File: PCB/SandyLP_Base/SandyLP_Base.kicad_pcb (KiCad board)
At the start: 2 copper layers, 275.5 x 80.3 mm, 229 parts, among them J1 Conn_01x10_Pin, J7 USB_C_Receptacle_USB2.0, J8 Conn_01x03, Q1 BSS138, SW1 BOOT, SW2 RESET, U1 NCP1117-3.3_SOT223, U2 RP2040, U3 W25Q128JVPIQ, Y1 12MHz

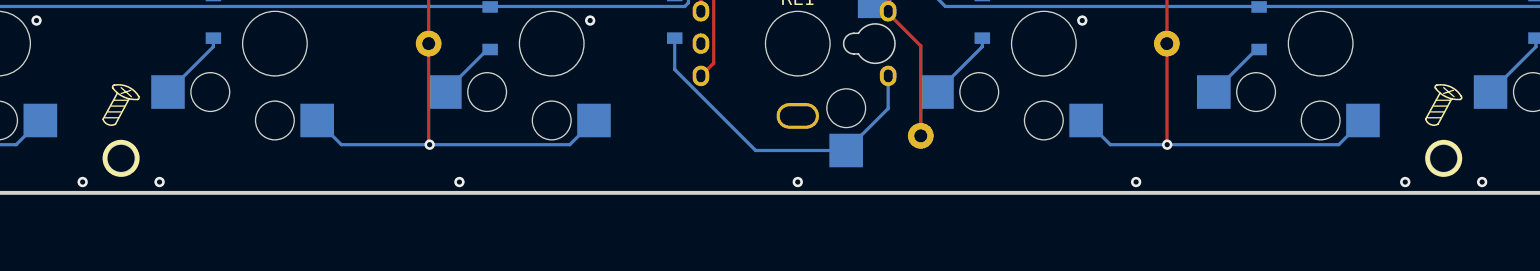
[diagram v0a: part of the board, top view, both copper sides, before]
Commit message: ネジ穴の位置を修正。
ネジ穴の位置が移動したので、シルク位置も調整。
GNDのVIAも位置調整。
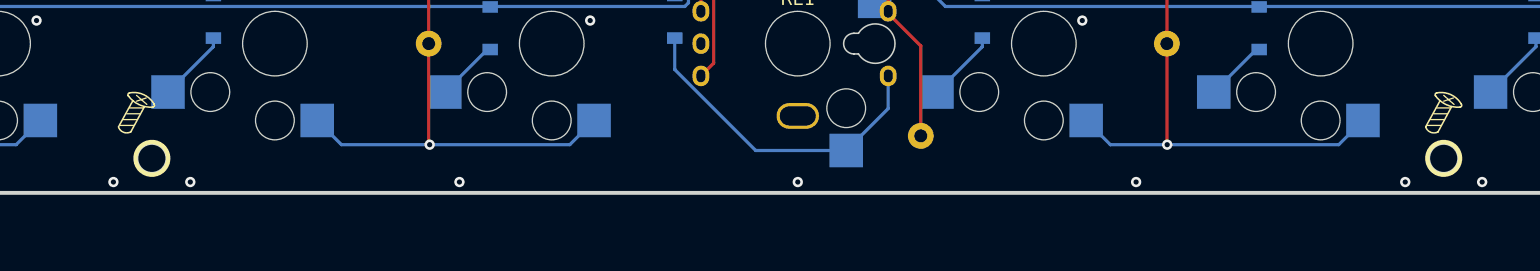
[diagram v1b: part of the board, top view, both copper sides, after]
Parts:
- moved H_btm_9 2.38 mm to (109.2, 112.1)
- moved REF** 1.88 mm to (207.9, 111.3)
- moved REF** 1.33 mm to (107.9, 111.1)
- moved REF** 0.84 mm to (106.7, 111.3)
- moved REF** 0.60 mm to (209.1, 111.1)
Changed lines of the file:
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@@
 		(locked yes)
 		(layer "F.Cu")
-		(at 106.783435 112.08778)
+		(at 109.164685 112.08778)
 		(descr "Mounting Hole 2.2mm, no annular, M2")
 		(tags "mounting hole 2.2mm no annular m2")
@@
 			(polygon
 				(pts
-					(xy 107.783435 109.88778) (xy 108.583435 110.48778) (xy 109.083435 111.28778) (xy 109.183435 112.08778)
-					(xy 109.083435 112.88778) (xy 108.583435 113.68778) (xy 107.783435 114.28778) (xy 106.783435 114.48778)
-					(xy 105.783435 114.28778) (xy 104.983435 113.68778) (xy 104.483435 112.88778) (xy 104.383435 112.08778)
-					(xy 104.483435 111.28778) (xy 104.983435 110.48778) (xy 105.783435 109.88778) (xy 106.783435 109.68778)
+					(xy 110.164685 109.88778) (xy 110.964685 110.48778) (xy 111.464685 111.28778) (xy 111.564685 112.08778)
+					(xy 111.464685 112.88778) (xy 110.964685 113.68778) (xy 110.164685 114.28778) (xy 109.164685 114.48778)
+					(xy 108.164685 114.28778) (xy 107.364685 113.68778) (xy 106.864685 112.88778) (xy 106.764685 112.08778)
+					(xy 106.864685 111.28778) (xy 107.364685 110.48778) (xy 108.164685 109.88778) (xy 109.164685 109.68778)
 				)
 			)
@@
 		(locked yes)
 		(layer "F.Cu")
-		(at 209.090034 110.540768)
+		(at 209.089876 111.136014)
 		(property "Reference" "REF**"
 			(at 0 0.5 0)
@@
 		(fp_arc
 			(start -0.378178 -1.358526)
-			(mid -0.787708 -1.474533)
+			(mid -0.787709 -1.474533)
 			(end -0.8 -1.9)
 			(stroke
@@
 		(locked yes)
 		(layer "F.Cu")
-		(at 106.696198 110.540768)
+		(at 107.886751 111.136014)
 		(property "Reference" "REF**"
 			(at 0 0.5 0)
@@
 		(fp_arc
 			(start -0.378178 -1.358526)
-			(mid -0.787708 -1.474533)
+			(mid -0.787709 -1.474533)
 			(end -0.8 -1.9)
 			(stroke
@@
 		(locked yes)
 		(layer "B.Cu")
-		(at 107.336573 110.673035 180)
+		(at 106.741188 111.268285 180)
 		(property "Reference" "REF**"
 			(at 0 -0.5 0)
@@
 		(locked yes)
 		(layer "B.Cu")
-		(at 209.730409 110.673035 180)
+		(at 207.944313 111.268285 180)
 		(property "Reference" "REF**"
 			(at 0 -0.5 0)
@@
 		)
 	)
+	(gr_line
+		(start 9.152185 110.347155)
+		(end 306.808435 110.347155)
+		(stroke
+			(width 0.1)
+			(type default)
+		)
+		(layer "Eco2.User")
+	)
 	(gr_text "#SandyLP_kbd DN0010, Base by @jpskenn\ngithub.com/jpskenn/SandyLP"
 		(locked yes)
@@
 	)
 	(via
-		(at 103.806942 113.919101)
+		(at 106.188194 113.919101)
 		(size 0.8)
 		(drill 0.4)
@@
 	)
 	(via
-		(at 109.760072 113.919101)
+		(at 112.141324 113.919097)
 		(size 0.8)
 		(drill 0.4)

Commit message: issue セカンダリスピーカーを削除 #25
- スピーカー関連削除
- 未使用となったGPIO12をテストポイントとしてアクセス可能に
- 付近の配線、GNDベタ調整
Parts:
- removed D35: D, locallib:D_SOD-123_Emphasized_Direction_Line_Reference_on_bottom
- removed LS2: Speaker, Buzzer_Beeper:Buzzer_Murata_PKMCS0909E
- removed R14: 1k, Resistor_SMD:R_0402_1005Metric
- added J2: Conn_01x01_Pin, TestPoint:TestPoint_THTPad_D1.0mm_Drill0.5mm, B.Cu at (58.6, 56.6)
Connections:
- U2 pad 15: Audio2 -> GPIO12
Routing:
- net Audio2: track 239.3 -> 0.00 mm, vias 4 -> 0
- net Net-(LS2-Pad1): track 5.42 -> 0.00 mm
- net row7: track 281.3 -> 275.9 mm
- net GPIO12: track 0.00 -> 2.97 mm
- net row4: track 327.7 -> 329.2 mm
- net row3: track 277.0 -> 277.7 mm
- net col0: track 150.4 -> 149.9 mm
- net GND: vias 143 -> 144

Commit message: LEDの位置を変更
周りの配線を調整
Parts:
- moved C19 4.26 mm to (282.9, 78.6), turned to 0 degrees
- moved C20 3.63 mm to (282.9, 83.4), turned to 0 degrees
- moved C21 3.32 mm to (282.9, 88.1), turned to 0 degrees
- moved C14 2.84 mm to (25.8, 78.6), turned to 0 degrees
- moved C15 1.76 mm to (25.8, 83.4), turned to 0 degrees
- moved L3 1.68 mm to (30.6, 88.9)
- moved L1 1.68 mm to (30.6, 79.4)
- moved L6 1.68 mm to (287.8, 88.9)
- moved L4 1.68 mm to (287.8, 79.4)
- moved L2 1.19 mm to (30.6, 84.2)
- moved L5 1.19 mm to (287.8, 84.2)
- moved C18 0.99 mm to (25.8, 88.1), turned to 0 degrees
- moved R11 0.41 mm to (37.7, 75.1)
- moved Q1 0.40 mm to (35.1, 75.6)
- moved R12 0.40 mm to (32.5, 75.0)
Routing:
- net LED_D_5V_CONNECTION: track 282.3 -> 277.9 mm
- net +5V: track 338.2 -> 334.4 mm
- net LED_D_5V: track 3.89 -> 5.93 mm
- net row4: track 329.2 -> 327.4 mm
- net col0: track 149.9 -> 149.2 mm
- net Net-(L4-DOUT): track 8.05 -> 7.36 mm
- net Net-(L5-DOUT): track 7.95 -> 7.36 mm
- net GND: vias 144 -> 145

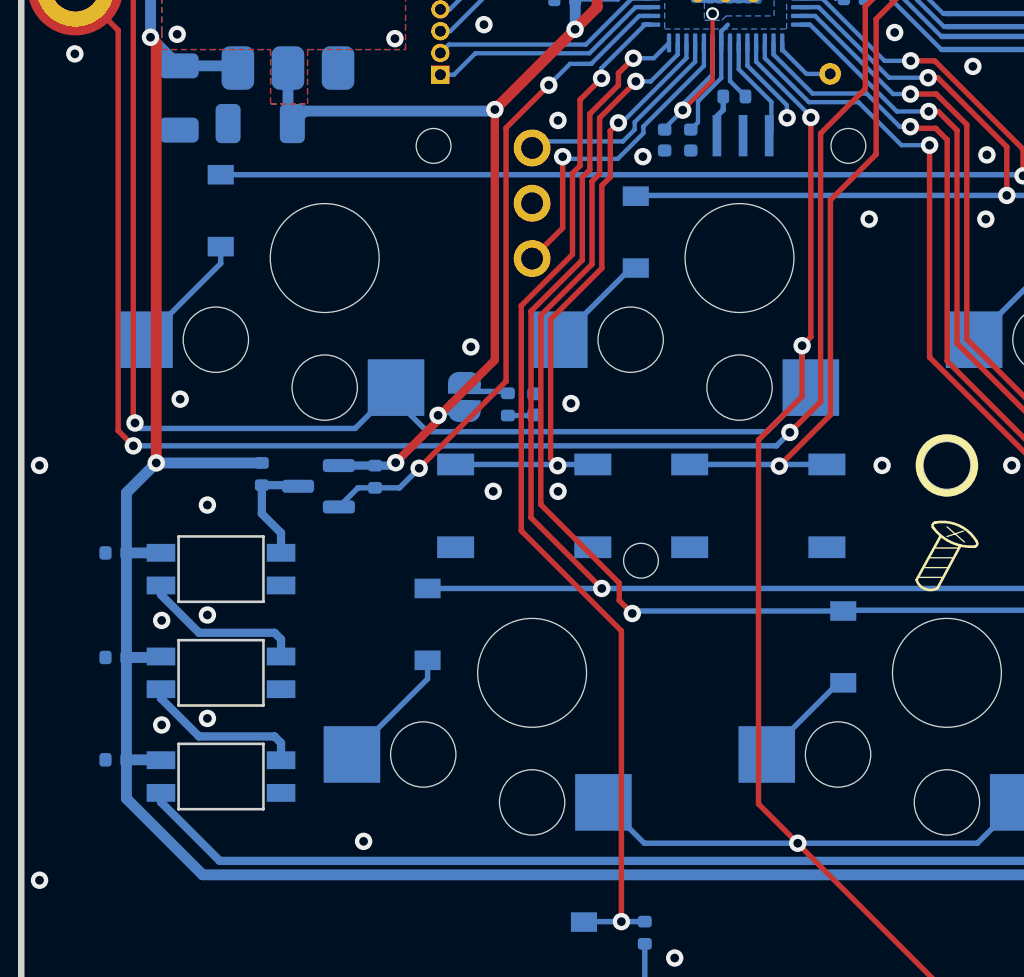
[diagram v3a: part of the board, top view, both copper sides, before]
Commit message: issue BOOTSELスイッチを両対応 #28
PTS810スイッチを隣に並べた。
RESETスイッチは削除して、ピンヘッダに出した。
LEDはサイズを変更。
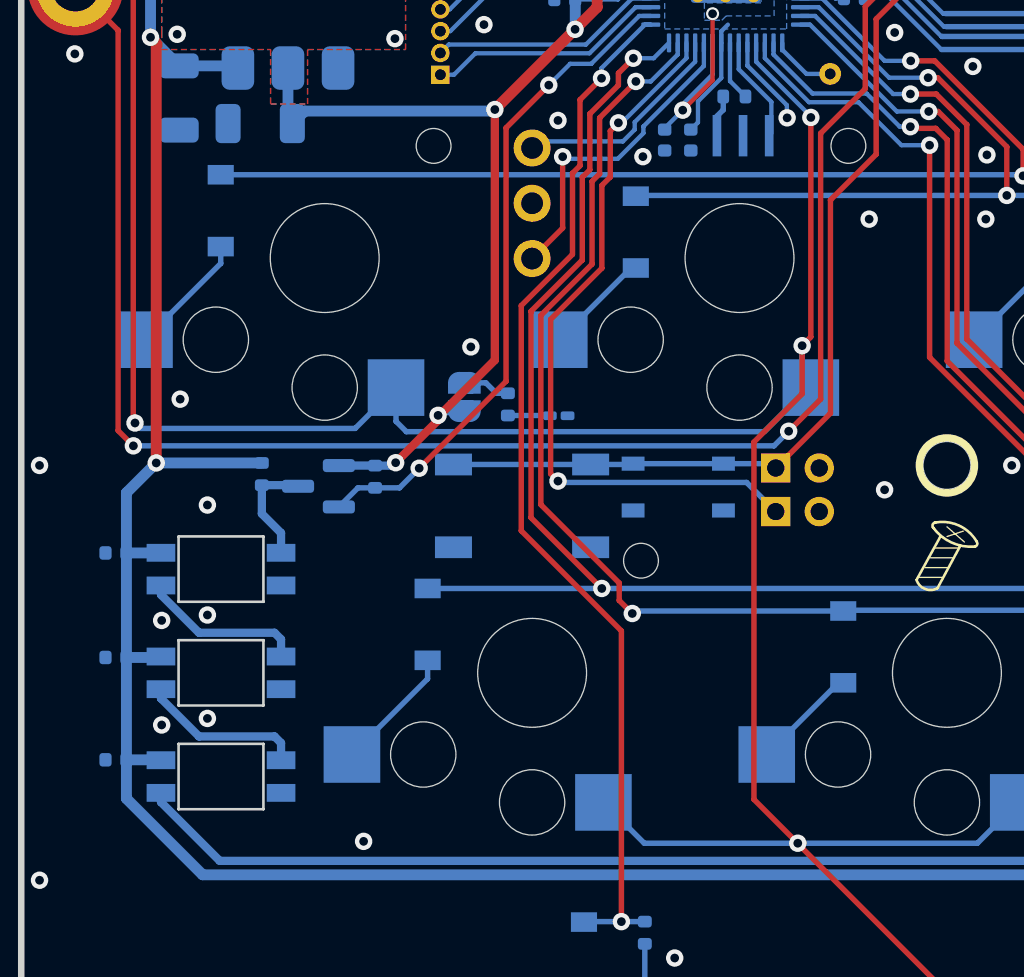
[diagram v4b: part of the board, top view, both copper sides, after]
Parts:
- removed SW2: RESET, Button_Switch_SMD:SW_SPST_TL3342
- added J3: Conn_02x02_Odd_Even, locallib:PinHeader_2x02_P2.00mm_Vertical_2pair, B.Cu at (56.1, 76.7)
- added SW3: BOOT_ALT, Button_Switch_SMD:SW_SPST_PTS810, B.Cu at (51.6, 75.6)
- STLED1: footprint LED_SMD:LED_0402_1005Metric -> LED_SMD:LED_0201_0603Metric_Pad0.64x0.40mm_HandSolder
- moved SW1 10.9 mm to (44.4, 76.5)
- moved STLED1 1.24 mm to (46.1, 72.3), turned to 180 degrees
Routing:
- net USB_BOOT: track 46.9 -> 55.6 mm, vias 2 -> 1
- net RESET: track 28.6 -> 33.5 mm
- net col0: track 149.2 -> 149.9 mm
- net Net-(STLED1-A): track 1.22 -> 1.93 mm
- net GND: vias 145 -> 142

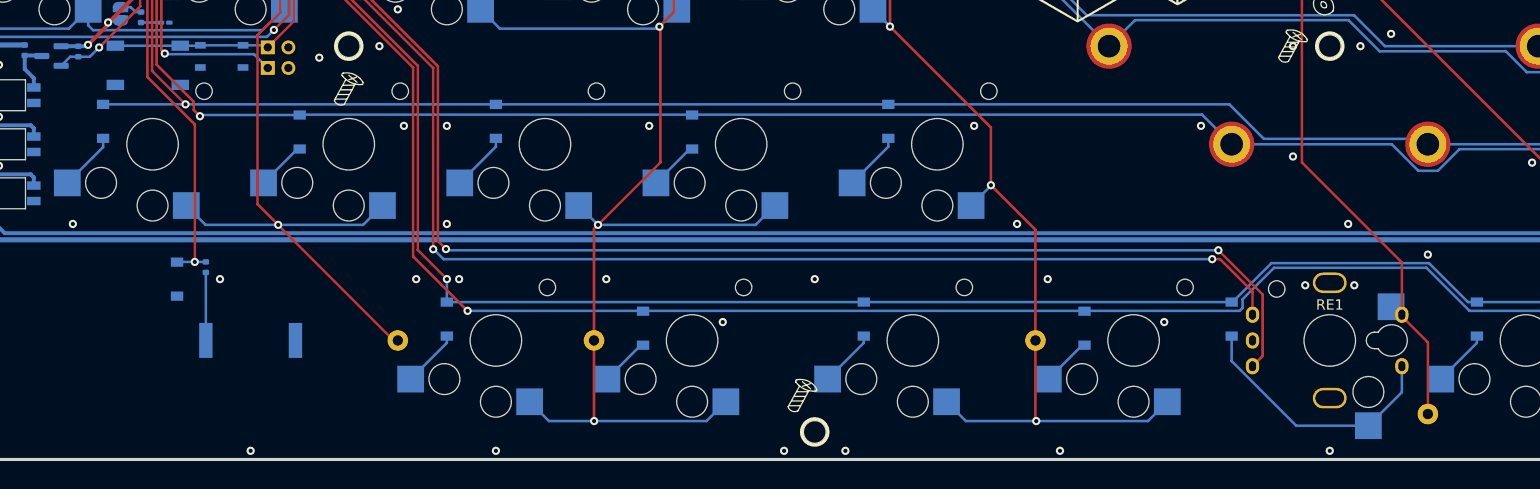
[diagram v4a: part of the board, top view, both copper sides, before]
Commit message: ロータリーエンコーダとダイオードが近すぎるので、少し離した。
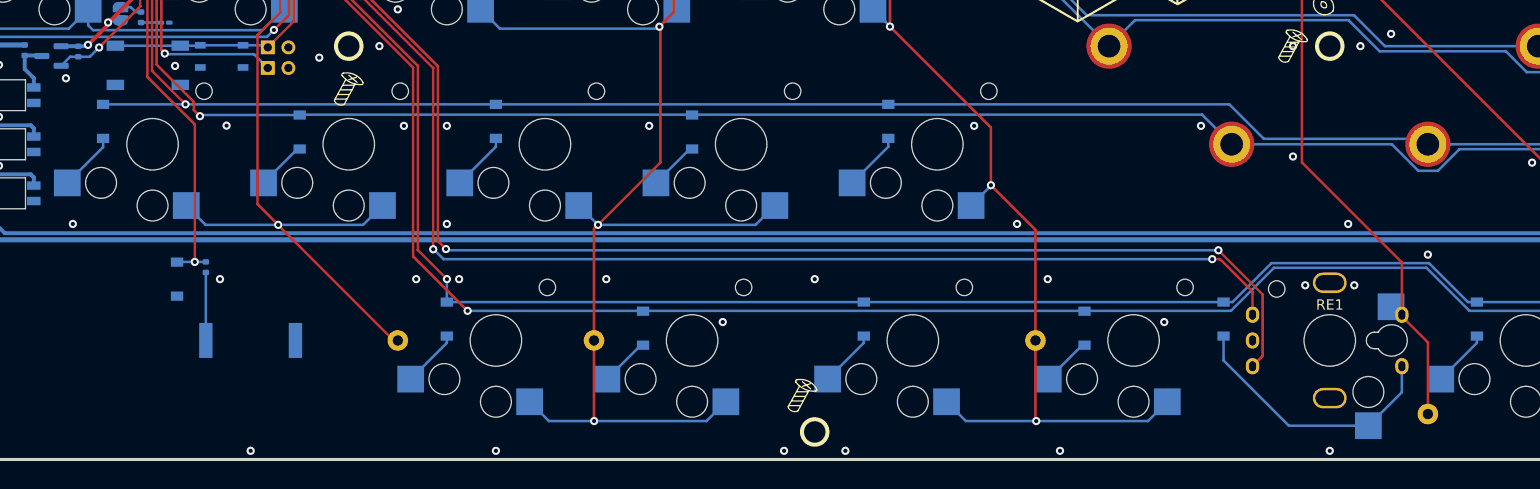
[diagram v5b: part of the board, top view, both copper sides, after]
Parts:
- moved D29 0.79 mm to (148.9, 101.1)
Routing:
- net Net-(D29-A): track 25.4 -> 26.2 mm
- net GND: vias 142 -> 145
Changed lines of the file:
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@@
 		(fp_arc
 			(start -0.378178 -1.358526)
-			(mid -0.787708 -1.474533)
+			(mid -0.787709 -1.474533)
 			(end -0.8 -1.9)
 			(stroke
@@
 		(fp_arc
 			(start -0.378178 -1.358526)
-			(mid -0.787708 -1.474533)
+			(mid -0.787709 -1.474533)
 			(end -0.8 -1.9)
 			(stroke
@@
 		(tags "Through hole pin header THT 2x02 2.00mm double row")
 		(property "Reference" "J3"
-			(at 1 2.06 360)
+			(at 1 2.06 0)
 			(layer "B.SilkS")
 			(effects
@@
 		)
 		(property "Value" "Conn_02x02_Odd_Even"
-			(at 1 -4.06 360)
+			(at 1 -4.06 0)
 			(layer "B.Fab")
 			(effects
@@
 		)
 		(property "Value" "LED_GREEN"
-			(at 0 -1.05 360)
+			(at 0 -1.05 0)
 			(layer "B.Fab")
 			(effects
@@
 		)
 		(fp_text user "${REFERENCE}"
-			(at 0 0.68 360)
+			(at 0 0.68 0)
 			(layer "B.Fab")
 			(effects
@@
 		(tags "SPST Button Switch")
 		(property "Reference" "SW3"
-			(at 0.675 2.6 360)
+			(at 0.675 2.6 0)
 			(layer "B.SilkS")
 			(effects
@@
 		)
 		(property "Value" "BOOT_ALT"
-			(at 0 -2.6 360)
+			(at 0 -2.6 0)
 			(layer "B.Fab")
 			(effects
@@
 		)
 		(fp_text user "${REFERENCE}"
-			(at 0 0 360)
+			(at 0 0 0)
 			(layer "B.Fab")
 			(effects
@@
 	(footprint "locallib:D_SOD-123_Emphasized_Direction_Line_Reference_on_bottom"
 		(layer "B.Cu")
-		(at 149.645935 101.128405 -90)
+		(at 148.858435 101.128405 -90)
 		(descr "SOD-123")
 		(tags "SOD-123")
@@
 	)
 	(segment
+		(start 135.39245 100.328765)
+		(end 149.576825 100.328765)
+		(width 0.25)
+		(layer "B.Cu")
+		(net 37)
+	)
+	(segment
 		(start 194.85567 100.328765)
 		(end 194.889685 100.36278)
@@
 	)
 	(segment
-		(start 150.426825 100.328765)
-		(end 150.708435 100.047155)
-		(width 0.25)
-		(layer "B.Cu")
-		(net 37)
-	)
-	(segment
-		(start 135.39245 100.328765)
-		(end 150.426825 100.328765)
+		(start 153.758435 96.147155)
+		(end 168.558435 96.147155)
 		(width 0.25)
 		(layer "B.Cu")
@@
 	)
 	(segment
-		(start 168.558435 96.147155)
-		(end 172.740045 100.328765)
-		(width 0.25)
-		(layer "B.Cu")
-		(net 37)
-	)
-	(segment
-		(start 153.758435 96.147155)
-		(end 168.558435 96.147155)
-		(width 0.25)
-		(layer "B.Cu")
-		(net 37)
-	)
-	(segment
 		(start 235.80531 99.928405)
 		(end 290.43656 99.928405)
@@
 	)
 	(segment
-		(start 150.708435 100.047155)
-		(end 150.708435 99.197155)
+		(start 235.33656 100.328405)
+		(end 235.370935 100.36278)
 		(width 0.25)
 		(layer "B.Cu")
@@
 	)
 	(segment
-		(start 235.33656 100.328405)
-		(end 235.370935 100.36278)
-		(width 0.25)
+		(start 59.858435 57.947155)
+		(end 61.833435 59.922155)
+		(width 0.2)
 		(layer "B.Cu")
 		(net 37)
@@
 	)
 	(segment
-		(start 150.708435 99.197155)
+		(start 149.576825 100.328765)
 		(end 153.758435 96.147155)
 		(width 0.25)
@@
 	)
 	(segment
-		(start 59.858435 57.947155)
-		(end 61.833435 59.922155)
-		(width 0.2)
-		(layer "B.Cu")
-		(net 37)
-	)
-	(segment
 		(start 61.833435 59.922155)
 		(end 63.124288 59.922155)
@@
 	)
 	(segment
-		(start 172.740045 100.328765)
-		(end 194.85567 100.328765)
-		(width 0.25)
-		(layer "B.Cu")
-		(net 37)
-	)
-	(segment
 		(start 55.558435 55.921701)
 		(end 57.583889 57.947155)
@@
 	)
 	(segment
+		(start 172.740045 100.328765)
+		(end 194.85567 100.328765)
+		(width 0.25)
+		(layer "B.Cu")
+		(net 37)
+	)
+	(segment
+		(start 168.558435 96.147155)
+		(end 172.740045 100.328765)
+		(width 0.25)
+		(layer "B.Cu")
+		(net 37)
+	)
+	(segment
 		(start 230.608435 84.61278)
 		(end 230.3876 84.61278)
@@
 	)
 	(segment
-		(start 149.645935 105.207623)
-		(end 149.645935 102.778405)
+		(start 155.190045 111.478765)
+		(end 148.858435 105.147155)
 		(width 0.25)
 		(layer "B.Cu")
@@
 	)
 	(segment
-		(start 155.917077 111.478765)
-		(end 149.645935 105.207623)
+		(start 162.920935 111.478765)
+		(end 166.170935 108.228765)
 		(width 0.25)
 		(layer "B.Cu")
@@
 	(segment
 		(start 162.920935 111.478765)
-		(end 166.170935 108.228765)
+		(end 155.190045 111.478765)
 		(width 0.25)
 		(layer "B.Cu")
@@
 	)
 	(segment
-		(start 162.920935 111.478765)
-		(end 155.917077 111.478765)
+		(start 148.858435 105.147155)
+		(end 148.858435 102.778405)
 		(width 0.25)
 		(layer "B.Cu")
@@
 	)
 	(segment
-		(start 60.230249 57.547155)
-		(end 61.755249 59.072155)
-		(width 0.2)
+		(start 172.589685 99.478405)
+		(end 168.808435 95.697155)
+		(width 0.25)
 		(layer "B.Cu")
 		(net 53)
 	)
 	(segment
-		(start 73.445935 99.478405)
-		(end 113.927185 99.478405)
+		(start 113.927185 99.478405)
+		(end 148.858435 99.478405)
 		(width 0.25)
 		(layer "B.Cu")
@@
 	)
 	(segment
-		(start 149.645935 99.478405)
+		(start 153.508435 95.697155)
 		(end 149.727185 99.478405)
 		(width 0.25)
@@
 	)
 	(segment
-		(start 149.727185 99.478405)
-		(end 153.508435 95.697155)
-		(width 0.25)
+		(start 60.230249 57.547155)
+		(end 61.755249 59.072155)
+		(width 0.2)
 		(layer "B.Cu")
 		(net 53)
 	)
 	(segment
-		(start 153.508435 95.697155)
-		(end 168.808435 95.697155)
+		(start 73.445935 99.478405)
+		(end 113.927185 99.478405)
 		(width 0.25)
 		(layer "B.Cu")
@@
 	)
 	(segment
+		(start 173.458435 99.478405)
+		(end 172.589685 99.478405)
+		(width 0.25)
+		(layer "B.Cu")
+		(net 53)
+	)
+	(segment
 		(start 55.958435 55.222155)
 		(end 55.958435 55.756015)
@@
 	)
 	(segment
+		(start 168.808435 95.697155)
+		(end 153.508435 95.697155)
+		(width 0.25)
+		(layer "B.Cu")
+		(net 53)
+	)
+	(segment
 		(start 73.445935 97.253405)
 		(end 73.453318 97.246022)
@@
 	)
 	(segment
+		(start 149.727185 99.478405)
+		(end 148.858435 99.478405)
+		(width 0.25)
+		(layer "B.Cu")
+		(net 53)
+	)
+	(segment
 		(start 216.320935 99.478405)
 		(end 173.458435 99.478405)
@@
 	)
 	(segment
-		(start 168.808435 95.697155)
-		(end 172.589685 99.478405)
-		(width 0.25)
-		(layer "B.Cu")
-		(net 53)
-	)
-	(segment
-		(start 172.589685 99.478405)
-		(end 173.458435 99.478405)
-		(width 0.25)
-		(layer "B.Cu")
-		(net 53)
-	)
-	(segment
-		(start 149.645935 99.478405)
-		(end 113.927185 99.478405)
-		(width 0.25)
-		(layer "B.Cu")
-		(net 53)
-	)
-	(segment
 		(start 57.749575 57.547155)
 		(end 60.230249 57.547155)
@@
 	)
 	(via
+		(at 36.458435 77.747155)
+		(size 0.8)
+		(drill 0.4)
+		(layers "F.Cu" "B.Cu")
+		(free yes)
+		(net 91)
+	)
+	(via
 		(at 27.858435 86.547155)
 		(size 0.8)
@@
 	)
 	(via
+		(at 52.058435 82.347155)
+		(size 0.8)
+		(drill 0.4)
+		(layers "F.Cu" "B.Cu")
+		(free yes)
+		(net 91)
+	)
+	(via
 		(at 63.395935 45.578405)
 		(size 0.8)
@@
 		(size 0.8)
 		(drill 0.4)
+		(layers "F.Cu" "B.Cu")
+		(free yes)
+		(net 91)
+	)
+	(via
+		(at 47.058435 76.547155)
+		(size 0.8)
+		(drill 0.4)
